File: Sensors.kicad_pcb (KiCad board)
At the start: 4 copper layers, 8 parts, among them U01 BMI270, U02 BMM150

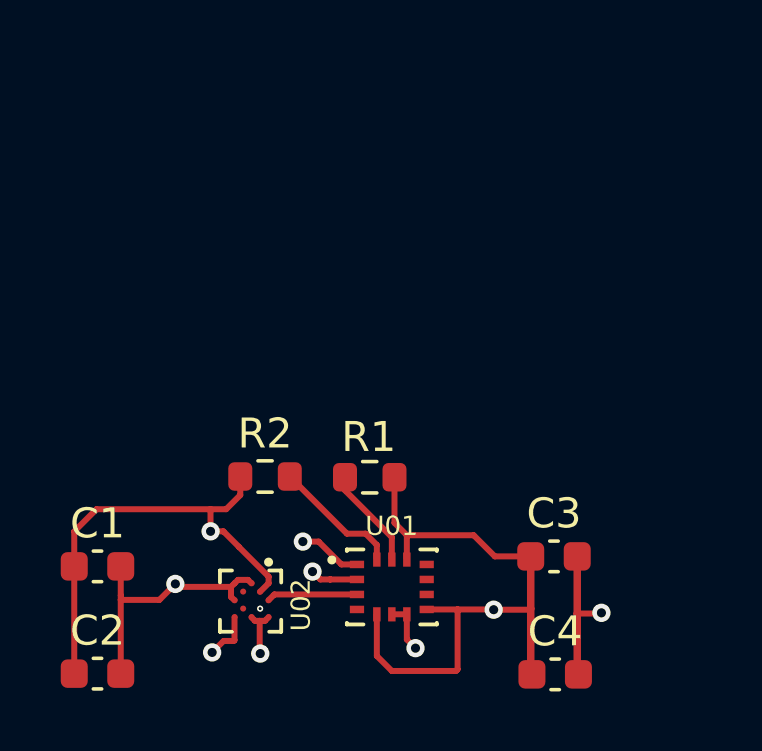
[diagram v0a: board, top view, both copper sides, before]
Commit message: Added Pin Headers to Schematic and PCB
6 pin connector for
sda
scl
gnd
3.3v
sdi
sck
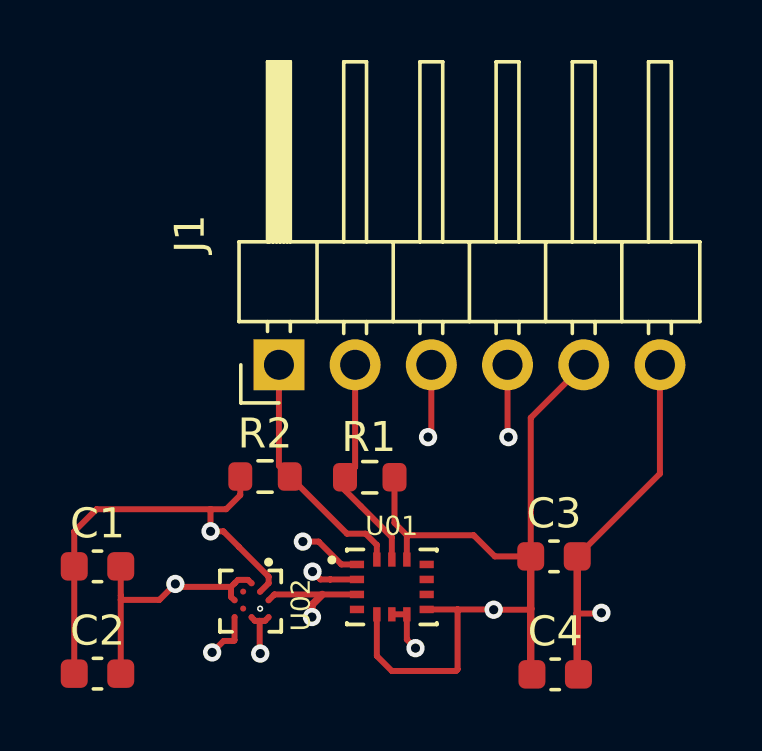
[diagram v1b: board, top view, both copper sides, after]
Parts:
- added J1: Conn_01x06_Female, Connector_PinHeader_2.54mm:PinHeader_1x06_P2.54mm_Horizontal, F.Cu at (82.1, 51.7)
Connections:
- C1 pad 1: SDA_IMU -> SCL_IMU
- C2 pad 1: SDA_IMU -> SCL_IMU
- C3 pad 1: SDA_IMU -> SCL_IMU
- C4 pad 1: SDA_IMU -> SCL_IMU
- R1 pad 1: SDA_IMU -> SCL_IMU
- R1 pad 2: Net-(R1-Pad2) -> SCL_IMU
- R2 pad 1: SDA_IMU -> SCL_IMU
- U01 pad 12: SDA_IMU -> SCL_IMU
- U01 pad 13: Net-(R1-Pad2) -> SCL_IMU
- U01 pad 5: SDA_IMU -> SCL_IMU
- U01 pad 8: SDA_IMU -> SCL_IMU
- U02 pad A1: SDA_IMU -> SCL_IMU
- U02 pad B2: SDA_IMU -> SCL_IMU
- U02 pad E5: SDA_IMU -> SCL_IMU
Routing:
- net SCL_IMU: track 0.00 -> 52.5 mm, vias 0 -> 3
- net SDA_IMU: track 38.1 -> 0.00 mm, vias 3 -> 0
- net GND: track 19.2 -> 26.8 mm
- net Net-(R2-Pad2): track 4.33 -> 8.21 mm
- net Net-(R1-Pad2): track 3.39 -> 0.00 mm
- net Net-(U01-Pad3): track 3.03 -> 6.37 mm, vias 0 -> 2
- net Net-(U01-Pad2): track 1.60 -> 4.07 mm, vias 2 -> 3
